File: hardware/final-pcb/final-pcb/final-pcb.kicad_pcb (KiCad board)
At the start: 4 copper layers, 85 x 55 mm, 7 parts, among them U1 ADS1299-4PAGR, U2 STM32L496ZGT6, U3 LTC3556EUFD-PBF

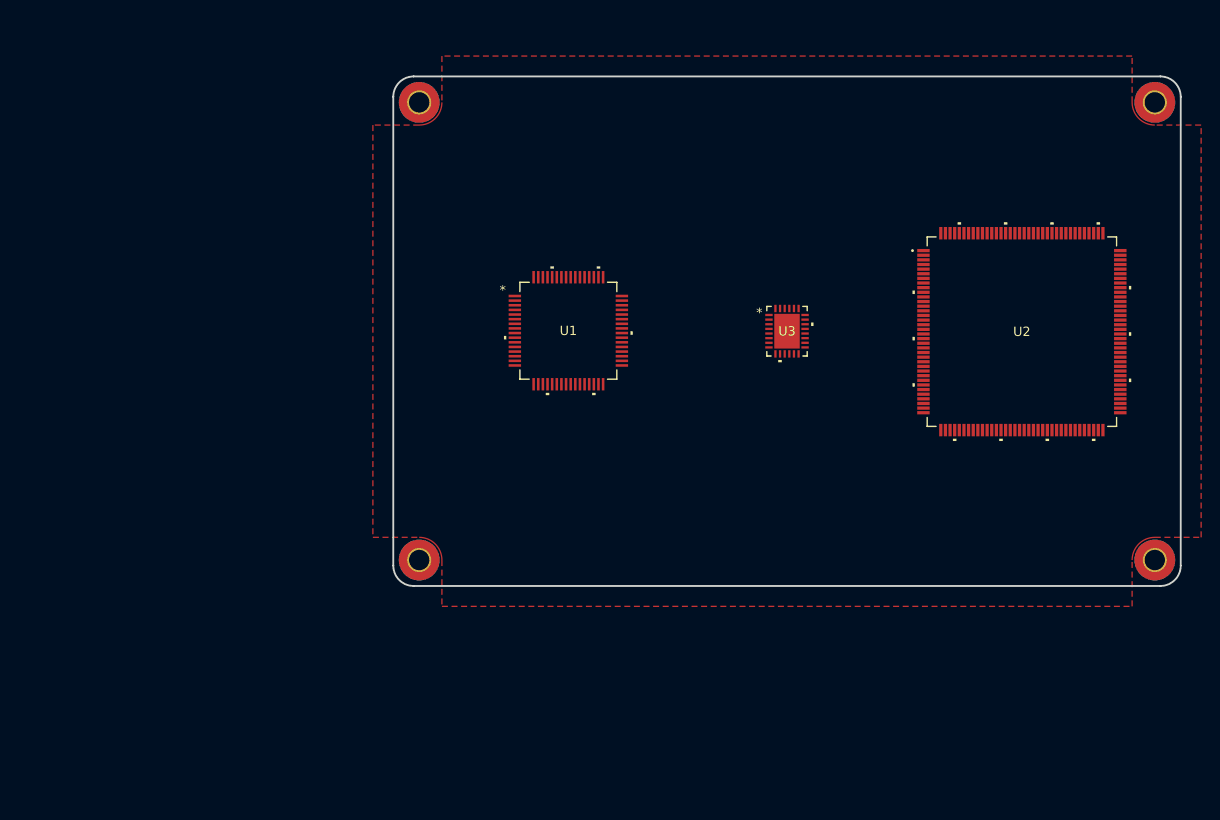
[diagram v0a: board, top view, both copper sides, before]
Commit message: Update sizes of schematics
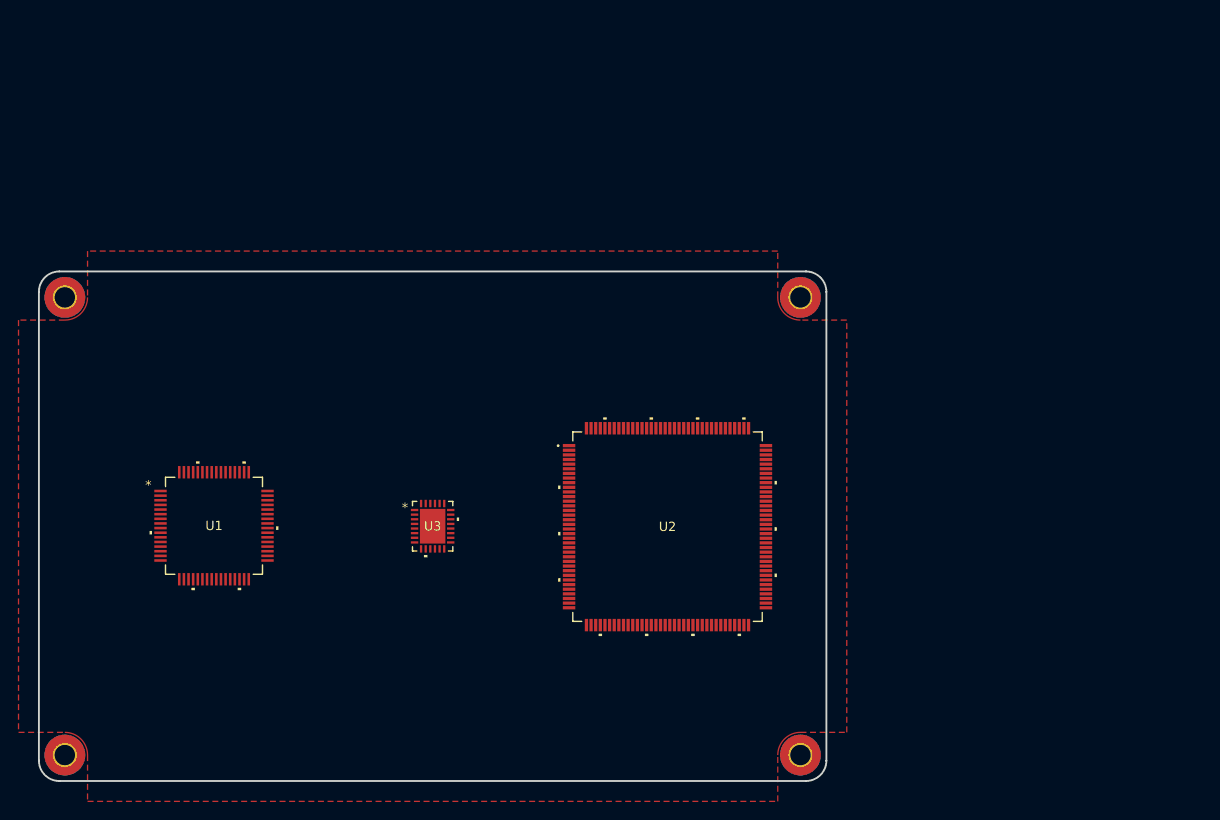
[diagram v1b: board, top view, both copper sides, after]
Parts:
- moved REF** 43.7 mm to (114.5, 118.2)
- moved REF** 43.7 mm to (114.5, 68.8)
- moved REF** 43.7 mm to (193.9, 118.2)
- moved REF** 43.7 mm to (193.9, 68.8)
- moved U1 43.7 mm to (130.7, 93.5)
- moved U2 43.7 mm to (179.6, 93.6)
- moved U3 43.7 mm to (154.2, 93.5)
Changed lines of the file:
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@@
 		(pad_to_mask_clearance 0)
 		(allow_soldermask_bridges_in_footprints no)
-		(grid_origin 192.5 72.5)
+		(grid_origin 154.25 93.55)
 		(pcbplotparams
 			(layerselection 0x00010fc_ffffffff)
@@
 	(footprint "MountingHole:MountingHole_2.2mm_M2_Pad_TopBottom"
 		(layer "F.Cu")
-		(at 152.8 97.2)
+		(at 114.55 118.25)
 		(descr "Mounting Hole 2.2mm, M2")
 		(tags "mounting hole 2.2mm m2")
@@
 	(footprint "hands-emg-lib:STM32L496ZGT6"
 		(layer "F.Cu")
-		(at 217.85 72.55)
+		(at 179.6 93.6)
 		(tags "STM32L496ZGT6 ")
 		(property "Reference" "U2"
@@
 	(footprint "hands-emg-lib:ADS1299-4PAGR"
 		(layer "F.Cu")
-		(at 168.9 72.45)
+		(at 130.65 93.5)
 		(tags "ADS1299-4PAGR ")
 		(property "Reference" "U1"
@@
 	(footprint "MountingHole:MountingHole_2.2mm_M2_Pad_TopBottom"
 		(layer "F.Cu")
-		(at 152.8 47.8)
+		(at 114.55 68.85)
 		(descr "Mounting Hole 2.2mm, M2")
 		(tags "mounting hole 2.2mm m2")
@@
 	(footprint "hands-emg-lib:LTC3556EUFD-PBF"
 		(layer "F.Cu")
-		(at 192.5 72.5)
+		(at 154.25 93.55)
 		(tags "LTC3556EUFD-PBF ")
 		(property "Reference" "U3"
@@
 	(footprint "MountingHole:MountingHole_2.2mm_M2_Pad_TopBottom"
 		(layer "F.Cu")
-		(at 232.2 97.2)
+		(at 193.95 118.25)
 		(descr "Mounting Hole 2.2mm, M2")
 		(tags "mounting hole 2.2mm m2")
@@
 	(footprint "MountingHole:MountingHole_2.2mm_M2_Pad_TopBottom"
 		(layer "F.Cu")
-		(at 232.2 47.8)
+		(at 193.95 68.85)
 		(descr "Mounting Hole 2.2mm, M2")
 		(tags "mounting hole 2.2mm m2")
@@
 	)
 	(gr_arc
-		(start 232.8 45)
-		(mid 234.355635 45.644365)
-		(end 235 47.2)
+		(start 194.55 66.05)
+		(mid 196.105635 66.694365)
+		(end 196.75 68.25)
 		(stroke
 			(width 0.2)
@@
 	)
 	(gr_arc
-		(start 152.2 100)
-		(mid 150.644365 99.355635)
-		(end 150 97.8)
+		(start 113.95 121.05)
+		(mid 112.394365 120.405635)
+		(end 111.75 118.85)
 		(stroke
 			(width 0.2)
@@
 	)
 	(gr_line
-		(start 150 97.8)
-		(end 150 47.2)
+		(start 111.75 118.85)
+		(end 111.75 68.25)
 		(stroke
 			(width 0.2)
@@
 	)
 	(gr_arc
-		(start 150 47.2)
-		(mid 150.644365 45.644365)
-		(end 152.2 45)
+		(start 111.75 68.25)
+		(mid 112.394365 66.694365)
+		(end 113.95 66.05)
 		(stroke
 			(width 0.2)
@@
 	)
 	(gr_line
-		(start 152.2 45)
-		(end 232.8 45)
+		(start 113.95 66.05)
+		(end 194.55 66.05)
 		(stroke
 			(width 0.2)
@@
 	)
 	(gr_line
-		(start 232.8 100)
-		(end 152.2 100)
+		(start 194.55 121.05)
+		(end 113.95 121.05)
 		(stroke
 			(width 0.2)
@@
 	)
 	(gr_arc
-		(start 235 97.8)
-		(mid 234.355635 99.355635)
-		(end 232.8 100)
+		(start 196.75 118.85)
+		(mid 196.105635 120.405635)
+		(end 194.55 121.05)
 		(stroke
 			(width 0.2)
@@
 	)
 	(gr_line
-		(start 235 47.2)
-		(end 235 97.8)
+		(start 196.75 68.25)
+		(end 196.75 118.85)
 		(stroke
 			(width 0.2)
@@
 	)
 	(gr_line
-		(start 150 72.5)
-		(end 235 72.5)
+		(start 111.75 93.55)
+		(end 196.75 93.55)
 		(stroke
 			(width 0.1)
@@
 	)
 	(gr_line
-		(start 192.5 45)
-		(end 192.5 100)
+		(start 154.25 66.05)
+		(end 154.25 121.05)
 		(stroke
 			(width 0.1)
@@
 		(polygon
 			(pts
-				(xy 147.8 94.75)
+				(xy 109.55 115.8)
 				(arc
-					(start 152.8 94.75)
-					(mid 154.532412 95.467588)
-					(end 155.25 97.2)
+					(start 114.55 115.8)
+					(mid 116.282412 116.517588)
+					(end 117 118.25)
 				)
-				(xy 155.25 102.2) (xy 229.75 102.2)
+				(xy 117 123.25) (xy 191.5 123.25)
 				(arc
-					(start 229.75 97.2)
-					(mid 230.467588 95.467588)
-					(end 232.2 94.75)
+					(start 191.5 118.25)
+					(mid 192.217588 116.517588)
+					(end 193.95 115.8)
 				)
-				(xy 237.2 94.75) (xy 237.2 50.25)
+				(xy 198.95 115.8) (xy 198.95 71.3)
 				(arc
-					(start 232.2 50.25)
-					(mid 230.467588 49.532412)
-					(end 229.75 47.8)
+					(start 193.95 71.3)
+					(mid 192.217588 70.582412)
+					(end 191.5 68.85)
 				)
-				(xy 229.75 42.8) (xy 155.25 42.8)
+				(xy 191.5 63.85) (xy 117 63.85)
 				(arc
-					(start 155.25 47.8)
-					(mid 154.532412 49.532412)
-					(end 152.8 50.25)
+					(start 117 68.85)
+					(mid 116.282412 70.582412)
+					(end 114.55 71.3)
 				)
-				(xy 147.8 50.25)
+				(xy 109.55 71.3)
 			)
 		)

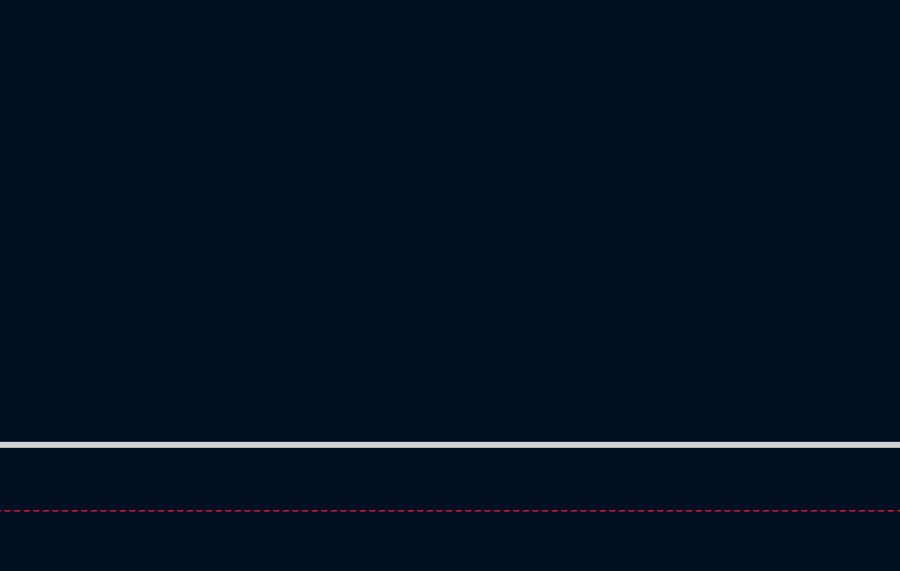
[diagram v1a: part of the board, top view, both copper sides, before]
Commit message: Silkscreen board, add USB connector
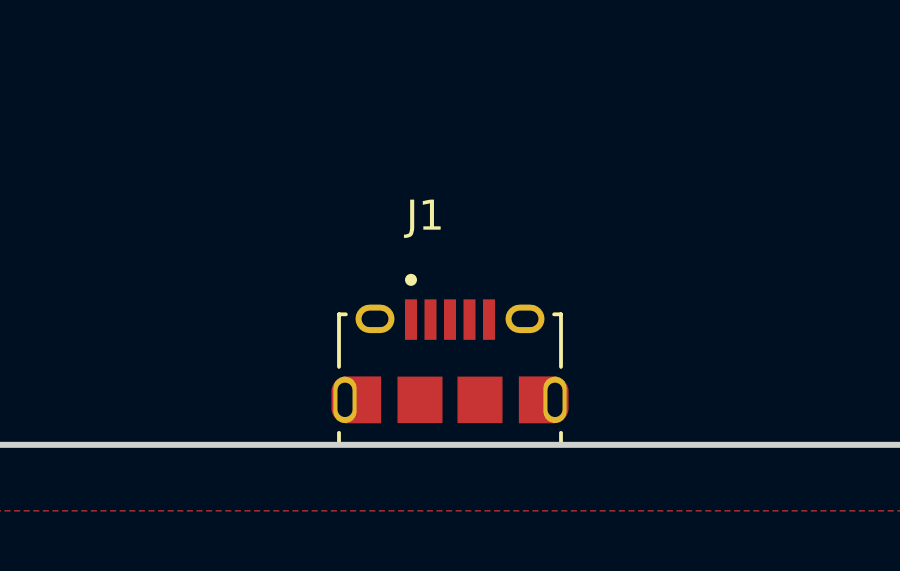
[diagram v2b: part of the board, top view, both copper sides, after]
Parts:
- added J1: 10118194-0001LF, hands-emg-lib:10118194-0001LF, F.Cu at (154.2, 119.5)
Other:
- board text added: "San Diego State University Smart Biomedical Systems Lab Senior Design Team 9 HANDS-EMG"

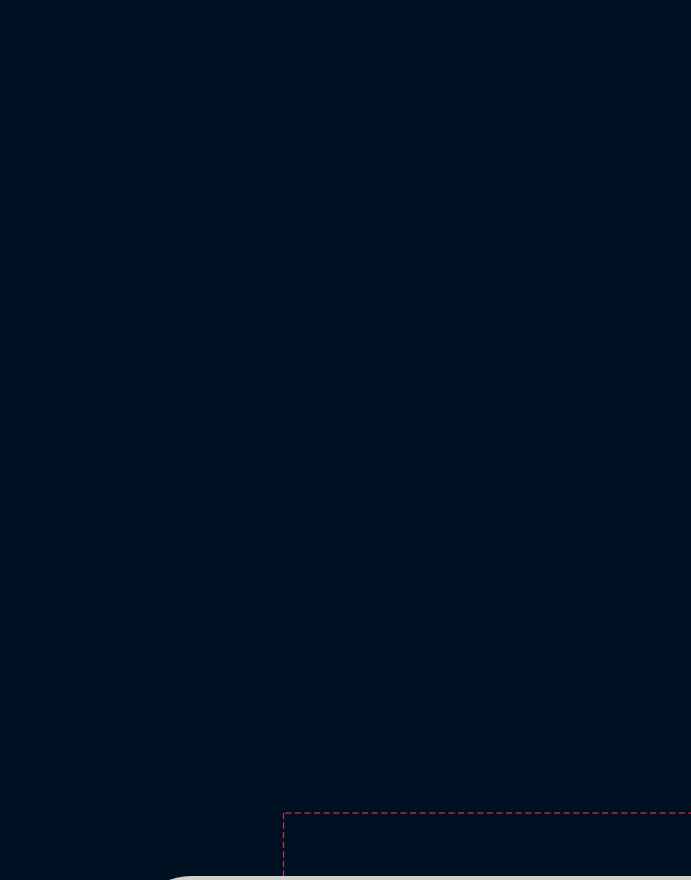
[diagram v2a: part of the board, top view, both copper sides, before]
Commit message: Add syms, footprints, 3dmodels for ADS and LTC boards
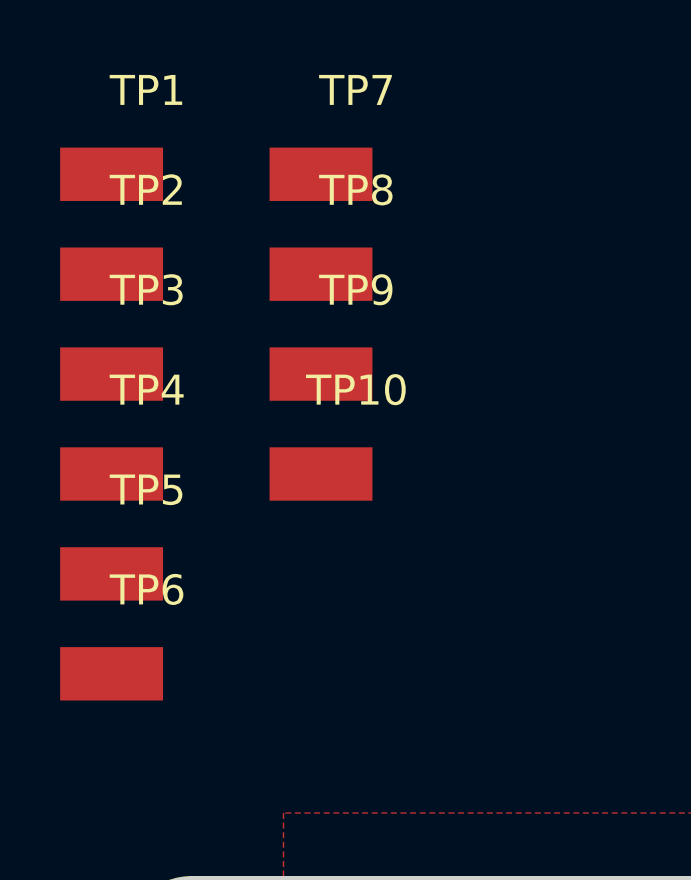
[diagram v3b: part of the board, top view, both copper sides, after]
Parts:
- added TP1: KEYSTONE_5015, hands-emg-lib:KEYSTONE_5015, F.Cu at (111.3, 42.6)
- added TP10: KEYSTONE_5015, hands-emg-lib:KEYSTONE_5015, F.Cu at (118.2, 52.5)
- added TP2: KEYSTONE_5015, hands-emg-lib:KEYSTONE_5015, F.Cu at (111.3, 45.9)
- added TP3: KEYSTONE_5015, hands-emg-lib:KEYSTONE_5015, F.Cu at (111.3, 49.2)
- added TP4: KEYSTONE_5015, hands-emg-lib:KEYSTONE_5015, F.Cu at (111.3, 52.5)
- added TP5: KEYSTONE_5015, hands-emg-lib:KEYSTONE_5015, F.Cu at (111.3, 55.9)
- added TP6: KEYSTONE_5015, hands-emg-lib:KEYSTONE_5015, F.Cu at (111.3, 59.2)
- added TP7: KEYSTONE_5015, hands-emg-lib:KEYSTONE_5015, F.Cu at (118.2, 42.6)
- added TP8: KEYSTONE_5015, hands-emg-lib:KEYSTONE_5015, F.Cu at (118.2, 45.9)
- added TP9: KEYSTONE_5015, hands-emg-lib:KEYSTONE_5015, F.Cu at (118.2, 49.2)
